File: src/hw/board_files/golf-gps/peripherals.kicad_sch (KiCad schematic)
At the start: 25 parts, among them J2 Micro_SD_Card, SW3 BTN_1, SW4 BTN_2, SW5 BTN_3, U4 NEO-M9N

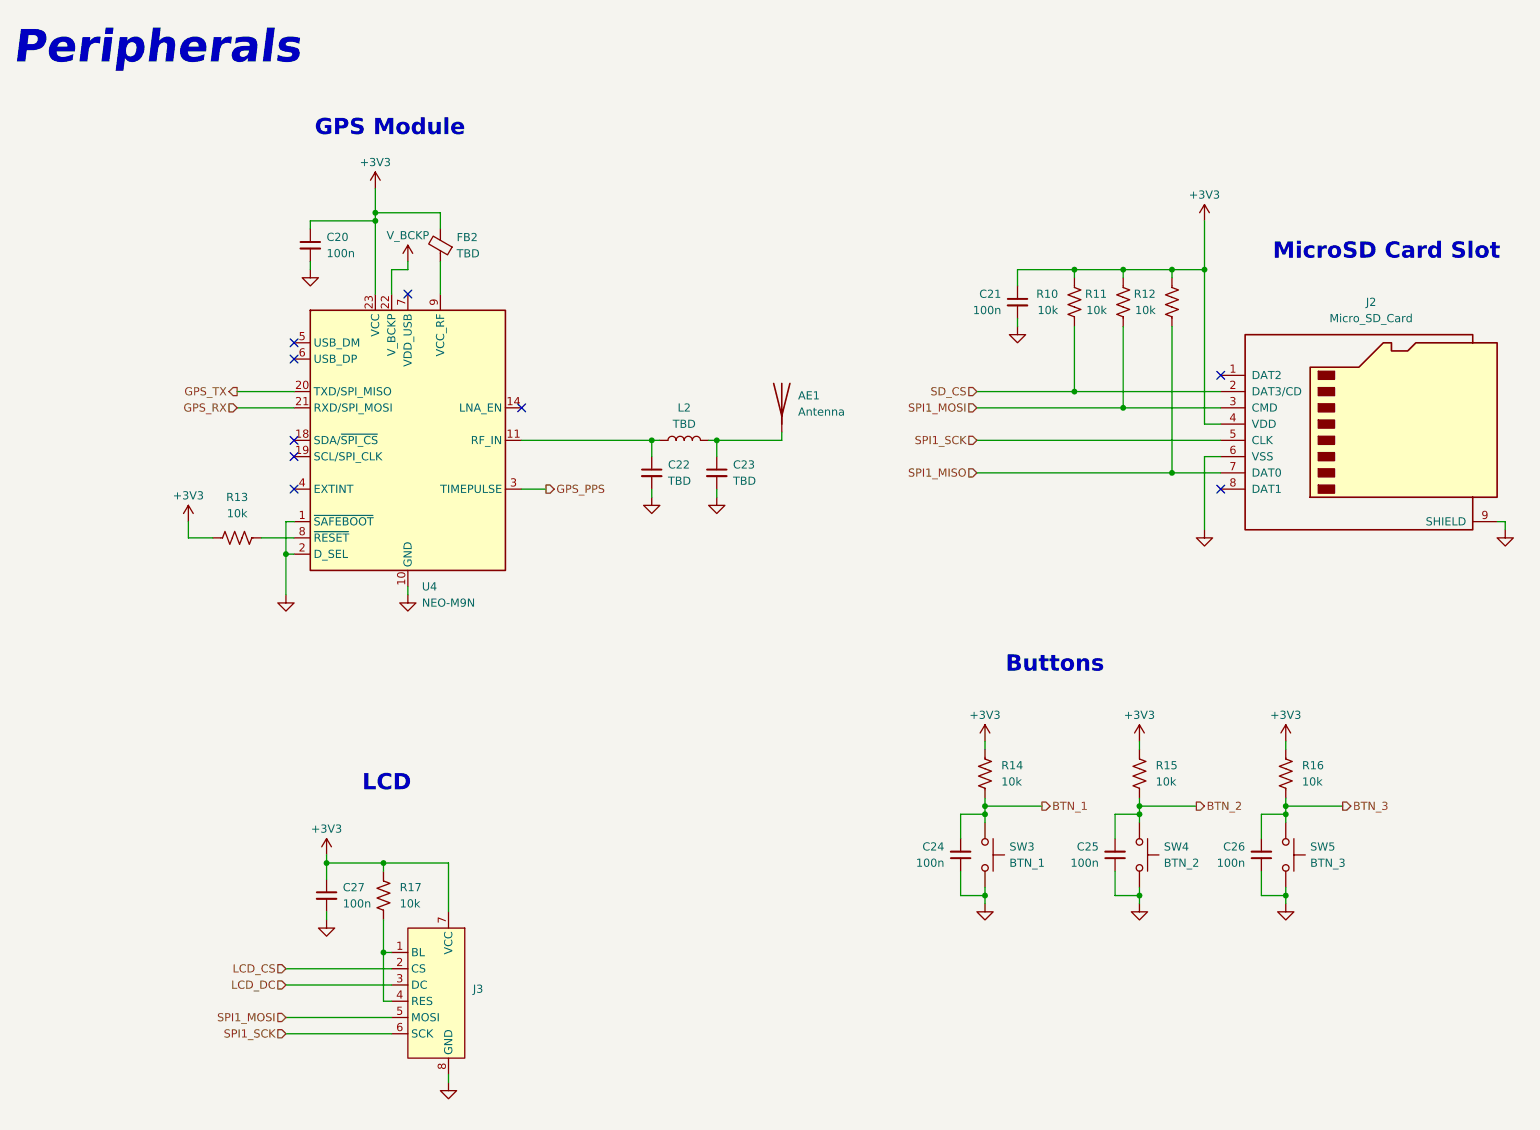
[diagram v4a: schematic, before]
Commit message: Updated pinout and spreadsheet, PCB changes
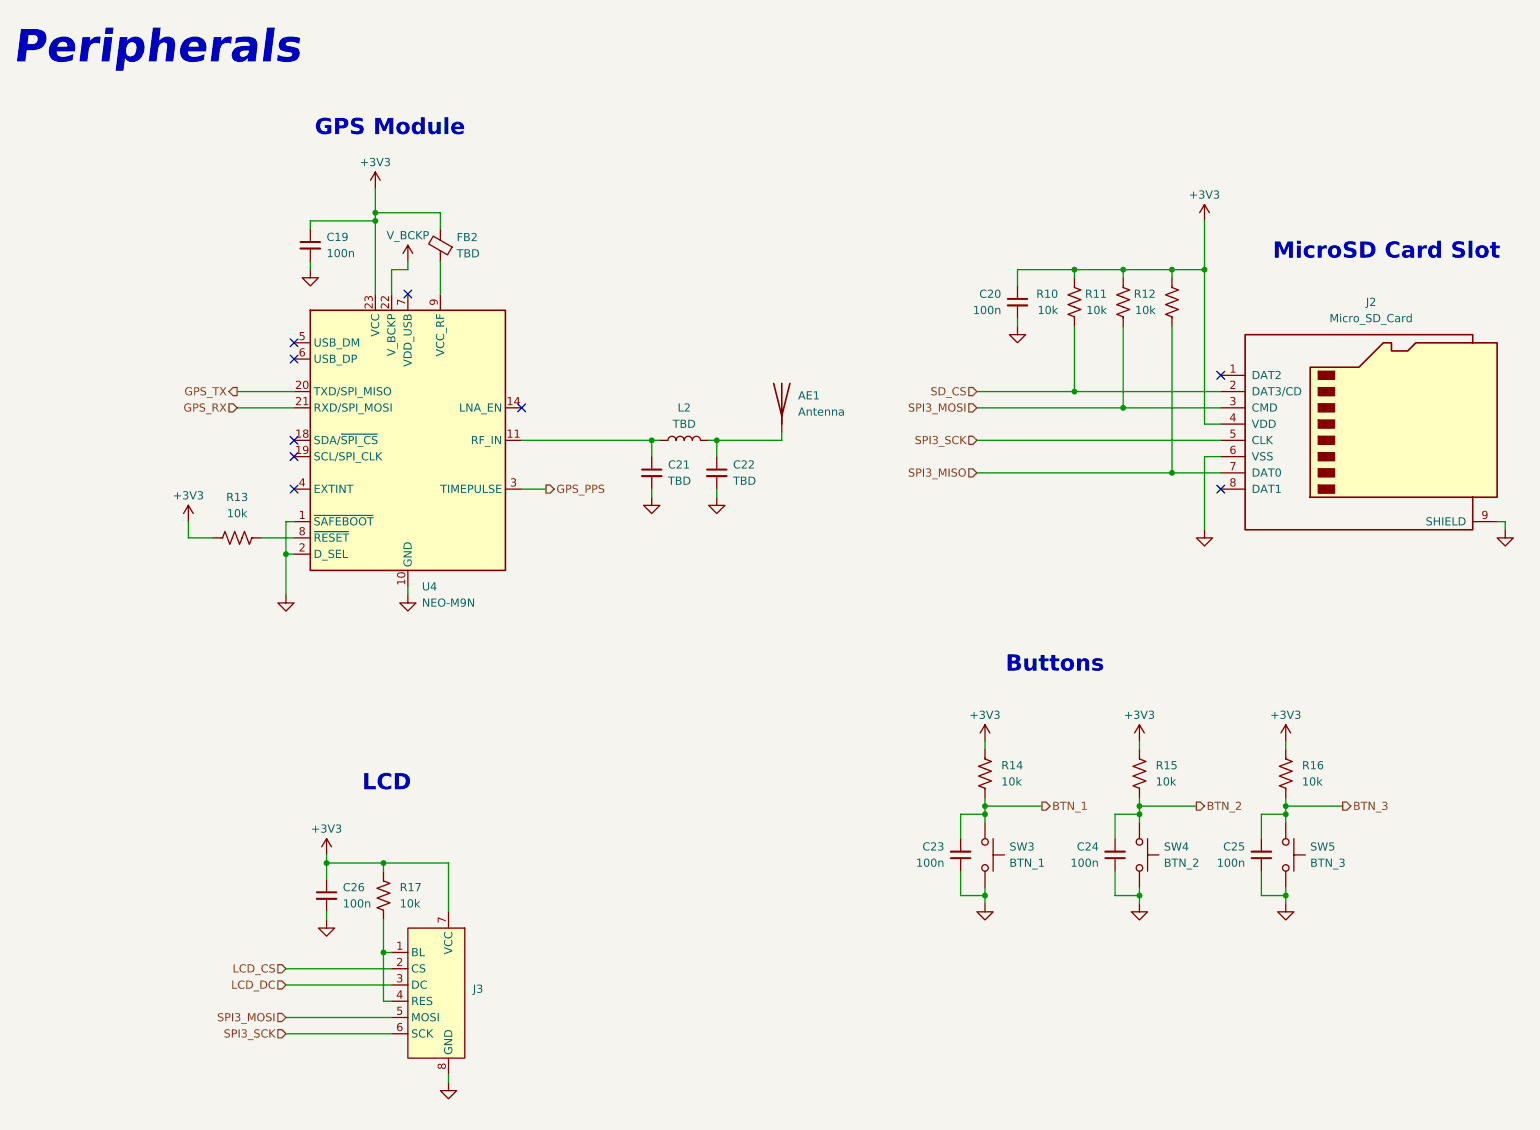
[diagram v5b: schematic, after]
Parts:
- renumbered C20 to C19, C21 to C20, C22 to C21, C23 to C22, C24 to C23, C25 to C24, C26 to C25, C27 to C26
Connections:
- net SPI1_MISO renamed SPI3_MISO
- net SPI1_MOSI renamed SPI3_MOSI
- net SPI1_SCK renamed SPI3_SCK

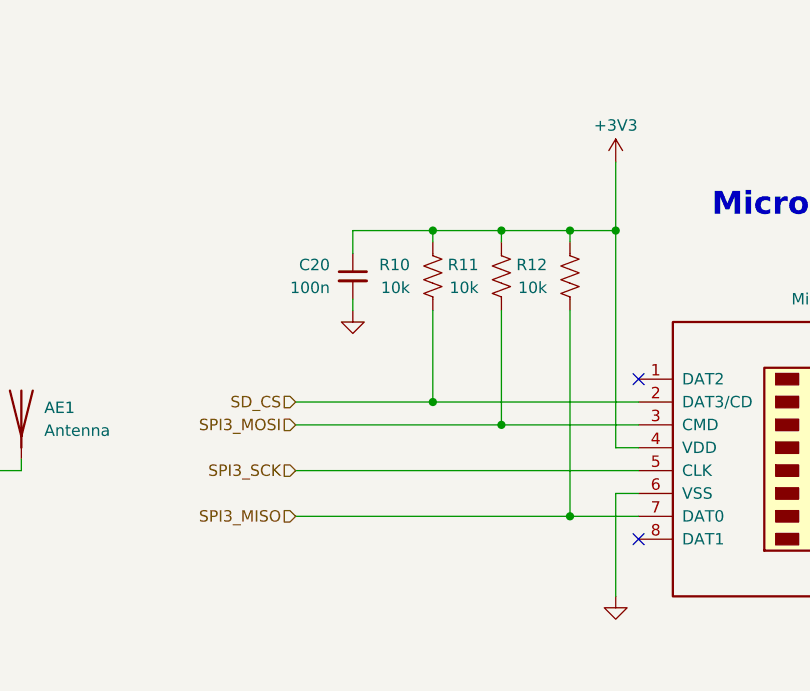
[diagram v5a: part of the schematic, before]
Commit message: Figured out general component placement and made progress routing. Removed pullup resistor from MOSI, MISO, and SCK lines
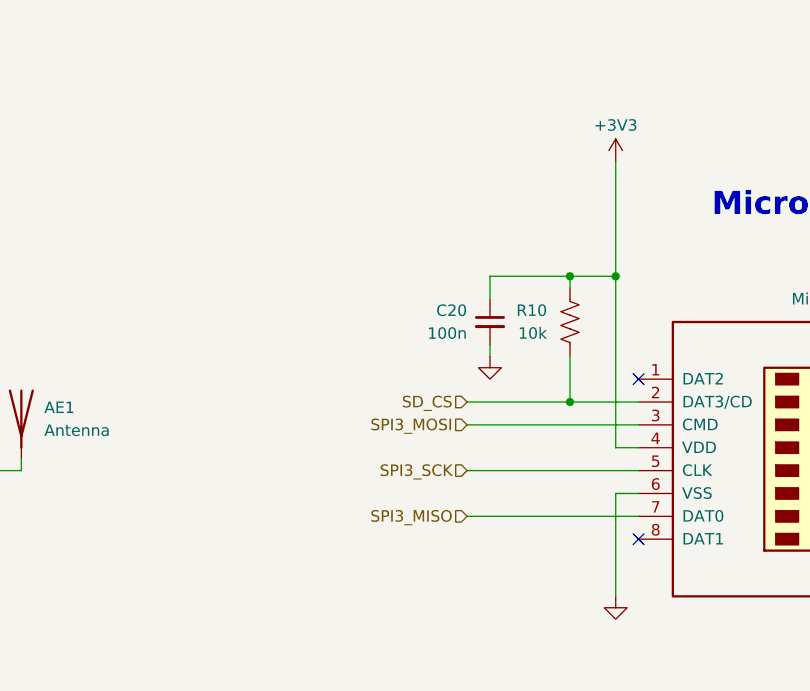
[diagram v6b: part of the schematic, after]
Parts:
- removed R11, R12: 10k, Resistor_SMD:R_0603_1608Metric, symbol Device:R_US
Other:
- moved on the sheet: C20, R10
